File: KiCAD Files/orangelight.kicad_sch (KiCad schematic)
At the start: 0 parts

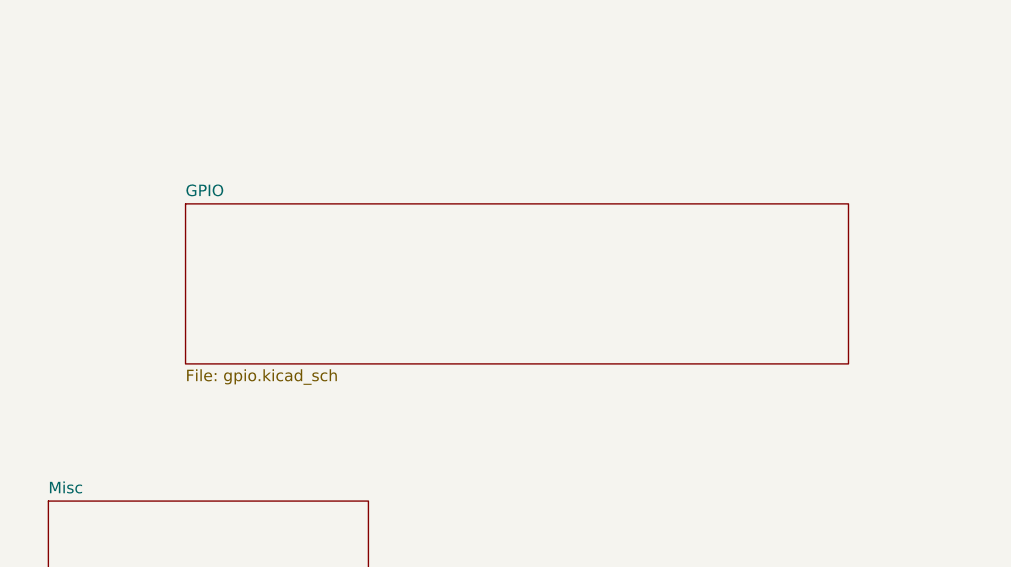
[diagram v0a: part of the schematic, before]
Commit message: more peripherals
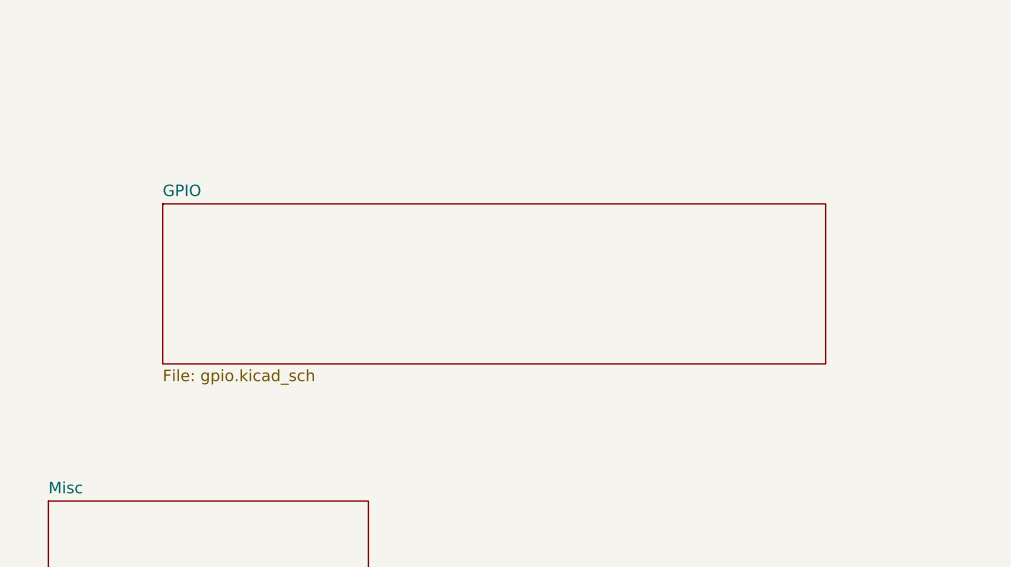
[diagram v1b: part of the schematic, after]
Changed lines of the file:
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@@
 	)
 	(sheet
-		(at 81.28 83.82)
+		(at 78.74 83.82)
 		(size 73.66 17.78)
 		(exclude_from_sim no)
@@
 		)
 		(property "Sheetname" "GPIO"
-			(at 81.28 83.1084 0)
+			(at 78.74 83.1084 0)
 			(effects
 				(font
@@
 		)
 		(property "Sheetfile" "gpio.kicad_sch"
-			(at 81.28 102.1846 0)
+			(at 78.74 102.1846 0)
 			(effects
 				(font
